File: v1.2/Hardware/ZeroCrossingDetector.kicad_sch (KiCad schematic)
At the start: 15 parts, among them Q17 MMBT3904, U12 OPA228

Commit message: Addition of firmware to v1.2(not tested)
+Addition of power tracking(with duty cycle control).
+Addition of resonance freq tracking(via proprietary algorithm relied on active and reactive power measurements)
+Quality factor monitoring
+Power boost when loaded(idle and loaded modes)
+Much better frequency resolution(less than 1Hz)
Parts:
- R49, R50: Link (none) -> https://ozdisan.com/passive-components/resistors/smt-smd-an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; Price 0.01964TL -> (none)

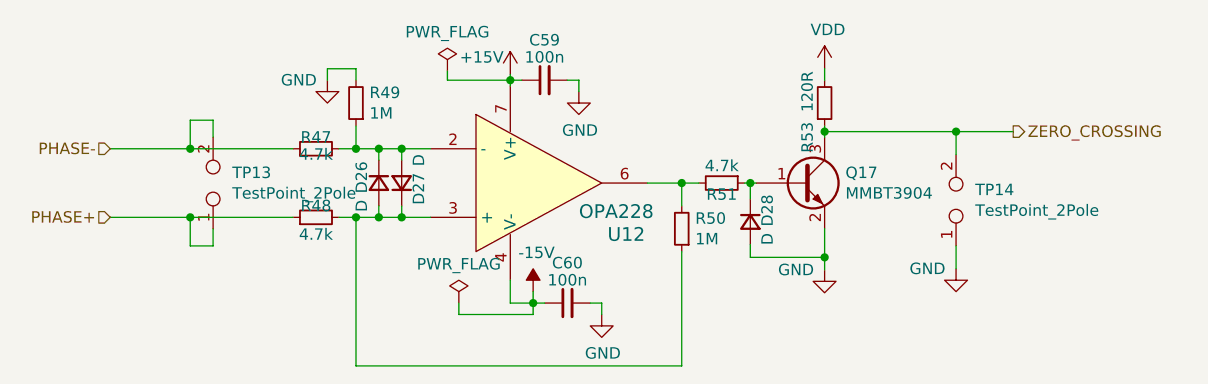
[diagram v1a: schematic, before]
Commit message: Start of rs485 communication interface development.
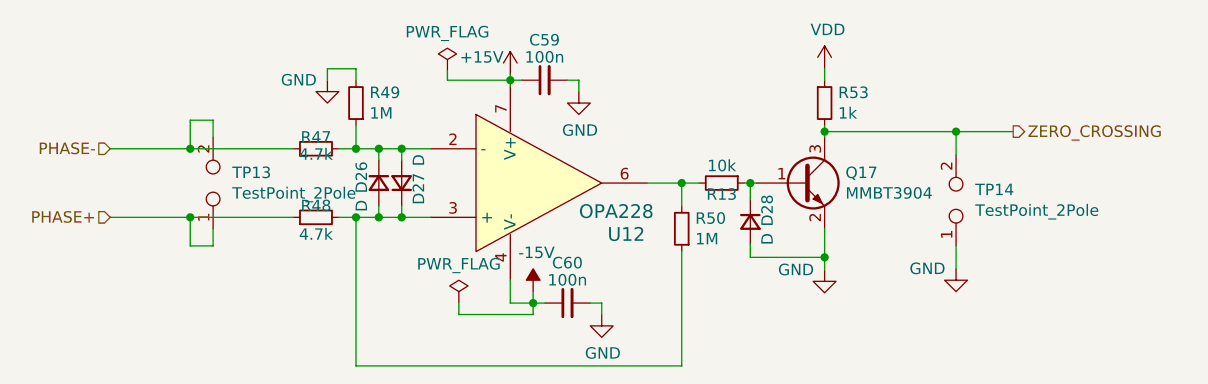
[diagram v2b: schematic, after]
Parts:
- removed R51: 4.7k, Resistor_SMD:R_0805_2012Metric, symbol Device:R_Small
- added R13: 10k, Resistor_SMD:R_0805_2012Metric, symbol Device:R_Small
- R53: value 120R -> 1k; footprint Resistor_SMD:R_0805_2012Metric -> Resistor_THT:R_Axial_DIN0204_L3.6mm_D1.6mm_P5.08mm_Horizontal; Link https://ozdisan.com/passive-components/resistors/smt-smd-an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 -> https://ozdisan.com/passive-components/resistors/tht-throug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; Price 0.01492TL -> 0.03898TL
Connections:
- net VDD: now also R53.1; no longer R53.2
- net ZERO_CROSSING: now also R53.2; no longer R53.1
- net at R50.2, U12.6: now also R13.2
- net at D28.1 (K), Q17.1 (B): now also R13.1
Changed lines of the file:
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@@
 (kicad_sch (version 20200618) (host eeschema "5.99.0-unknown-f3f1740~101~ubuntu18.04.1")
-  (page 1 8)
+  (page 8 8)
   (paper "A4")
   (junction (at 98.425 83.82) (diameter 0) (color 0 0 0 0))
@@
     (effects (font (size 1.27 1.27)) (justify left))
   )
-  (symbol (lib_id "power:PWR_FLAG") (at 127 75.184 0) (unit 1)
+  (symbol (lib_id "power:PWR_FLAG") (at 127 75.184 0)
     (in_bom yes) (on_board yes)
     (property "Reference" "#FLG0123" (id 0) (at 127 73.279 0)
@@
     )
   )
-  (symbol (lib_id "power:PWR_FLAG") (at 128.27 100.965 0) (unit 1)
+  (symbol (lib_id "power:PWR_FLAG") (at 128.27 100.965 0)
     (in_bom yes) (on_board yes)
     (property "Reference" "#FLG0122" (id 0) (at 128.27 99.06 0)
@@
     )
   )
-  (symbol (lib_id "power:+15V") (at 133.985 75.565 0) (unit 1)
+  (symbol (lib_id "power:+15V") (at 133.985 75.565 0)
     (in_bom yes) (on_board yes)
     (property "Reference" "#PWR059" (id 0) (at 133.985 79.375 0)
@@
     )
   )
-  (symbol (lib_id "power:-15V") (at 136.525 99.695 0) (unit 1)
+  (symbol (lib_id "power:-15V") (at 136.525 99.695 0)
     (in_bom yes) (on_board yes)
     (property "Reference" "#PWR060" (id 0) (at 136.525 97.155 0)
@@
     )
   )
-  (symbol (lib_id "power:VDD") (at 168.91 74.93 0) (unit 1)
+  (symbol (lib_id "power:VDD") (at 168.91 74.93 0)
     (in_bom yes) (on_board yes)
     (property "Reference" "#PWR075" (id 0) (at 168.91 78.74 0)
@@
     )
   )
-  (symbol (lib_id "power:GND") (at 113.665 76.2 0) (unit 1)
+  (symbol (lib_id "power:GND") (at 113.665 76.2 0)
     (in_bom yes) (on_board yes)
     (property "Reference" "#PWR058" (id 0) (at 113.665 82.55 0)
@@
     )
   )
-  (symbol (lib_id "power:GND") (at 141.605 77.47 0) (unit 1)
+  (symbol (lib_id "power:GND") (at 141.605 77.47 0)
     (in_bom yes) (on_board yes)
     (property "Reference" "#PWR061" (id 0) (at 141.605 83.82 0)
@@
     )
   )
-  (symbol (lib_id "power:GND") (at 144.145 102.235 0) (unit 1)
+  (symbol (lib_id "power:GND") (at 144.145 102.235 0)
     (in_bom yes) (on_board yes)
     (property "Reference" "#PWR062" (id 0) (at 144.145 108.585 0)
@@
     )
   )
-  (symbol (lib_id "power:GND") (at 168.91 97.282 0) (unit 1)
+  (symbol (lib_id "power:GND") (at 168.91 97.282 0)
     (in_bom yes) (on_board yes)
     (property "Reference" "#PWR065" (id 0) (at 168.91 103.632 0)
@@
     )
   )
-  (symbol (lib_id "power:GND") (at 183.515 97.155 0) (unit 1)
+  (symbol (lib_id "power:GND") (at 183.515 97.155 0)
     (in_bom yes) (on_board yes)
     (property "Reference" "#PWR0133" (id 0) (at 183.515 103.505 0)
@@
     )
   )
-  (symbol (lib_id "Device:R_Small") (at 112.395 83.82 90) (unit 1)
+  (symbol (lib_id "Device:R_Small") (at 112.395 83.82 90)
     (in_bom yes) (on_board yes)
     (property "Reference" "R47" (id 0) (at 112.395 82.55 90))
@@
     )
   )
-  (symbol (lib_id "Device:R_Small") (at 112.395 91.44 90) (unit 1)
+  (symbol (lib_id "Device:R_Small") (at 112.395 91.44 90)
     (in_bom yes) (on_board yes)
     (property "Reference" "R48" (id 0) (at 112.395 90.17 90))
@@
     )
   )
-  (symbol (lib_name "Device:R_Small_2") (lib_id "Device:R_Small") (at 116.84 78.74 180) (unit 1)
+  (symbol (lib_name "Device:R_Small_2") (lib_id "Device:R_Small") (at 116.84 78.74 180)
     (in_bom yes) (on_board yes)
     (property "Reference" "R49" (id 0) (at 118.3386 77.597 0)
@@
     )
   )
-  (symbol (lib_name "Device:R_Small_3") (lib_id "Device:R_Small") (at 153.035 92.71 180) (unit 1)
+  (symbol (lib_name "Device:R_Small_3") (lib_id "Device:R_Small") (at 153.035 92.71 180)
     (in_bom yes) (on_board yes)
     (property "Reference" "R50" (id 0) (at 154.5336 91.567 0)
@@
     )
   )
-  (symbol (lib_id "Device:R_Small") (at 157.48 87.63 270) (unit 1)
-    (in_bom yes) (on_board yes)
-    (property "Reference" "R51" (id 0) (at 157.48 88.9 90))
-    (property "Value" "4.7k" (id 1) (at 157.48 85.725 90))
+  (symbol (lib_name "Device:R_Small_7") (lib_id "Device:R_Small") (at 157.48 87.63 270)
+    (in_bom yes) (on_board yes)
+    (property "Reference" "R13" (id 0) (at 157.48 88.9 90))
+    (property "Value" "10k" (id 1) (at 157.48 85.725 90))
     (property "Footprint" "Resistor_SMD:R_0805_2012Metric" (id 2) (at 157.48 87.63 0)
       (effects (font (size 1.27 1.27)) hide)
@@
       (effects (font (size 1.27 1.27)) hide)
     )
-    (property "Link" "https://ozdisan.com/passive-components/resistors/smt-smd-and-chip-resistors/0805S8F4701T5E" (id 4) (at 157.48 87.63 90)
-      (effects (font (size 1.27 1.27)) hide)
-    )
-    (property "Price" "0.01955TL" (id 5) (at 157.48 87.63 90)
-      (effects (font (size 1.27 1.27)) hide)
-    )
-  )
-  (symbol (lib_name "Device:R_Small_1") (lib_id "Device:R_Small") (at 168.91 78.74 0) (mirror x) (unit 1)
-    (in_bom yes) (on_board yes)
-    (property "Reference" "R53" (id 0) (at 167.005 82.55 90))
-    (property "Value" "120R" (id 1) (at 167.005 77.47 90))
-    (property "Footprint" "Resistor_SMD:R_0805_2012Metric" (id 2) (at 168.91 78.74 0)
+    (property "Link" "https://ozdisan.com/passive-components/resistors/smt-smd-and-chip-resistors/0805S8J0103T5E" (id 4) (at 157.48 87.63 90)
+      (effects (font (size 1.27 1.27)) hide)
+    )
+    (property "Price" "0.01518TL" (id 5) (at 157.48 87.63 90)
+      (effects (font (size 1.27 1.27)) hide)
+    )
+  )
+  (symbol (lib_name "Device:R_Small_4") (lib_id "Device:R_Small") (at 168.91 78.74 0) (unit 1)
+    (in_bom yes) (on_board yes)
+    (property "Reference" "R53" (id 0) (at 170.4086 77.597 0)
+      (effects (font (size 1.27 1.27)) (justify left))
+    )
+    (property "Value" "1k" (id 1) (at 170.4086 79.883 0)
+      (effects (font (size 1.27 1.27)) (justify left))
+    )
+    (property "Footprint" "Resistor_THT:R_Axial_DIN0204_L3.6mm_D1.6mm_P5.08mm_Horizontal" (id 2) (at 168.91 78.74 0)
       (effects (font (size 1.27 1.27)) hide)
     )
@@
       (effects (font (size 1.27 1.27)) hide)
     )
-    (property "Link" "https://ozdisan.com/passive-components/resistors/smt-smd-and-chip-resistors/0805S8J0121T5E" (id 4) (at 168.91 78.74 90)
-      (effects (font (size 1.27 1.27)) hide)
-    )
-    (property "Price" "0.01492TL" (id 5) (at 168.91 78.74 90)
-      (effects (font (size 1.27 1.27)) hide)
-    )
-  )
-  (symbol (lib_id "Device:D_Small") (at 119.38 87.63 90) (mirror x) (unit 1)
+    (property "Link" "https://ozdisan.com/passive-components/resistors/tht-through-hole-resistors/CFR0W8J0102A50" (id 4) (at 168.91 78.74 0)
+      (effects (font (size 1.27 1.27)) hide)
+    )
+    (property "Price" "0.03898TL" (id 5) (at 168.91 78.74 0)
+      (effects (font (size 1.27 1.27)) hide)
+    )
+  )
+  (symbol (lib_id "Device:D_Small") (at 119.38 87.63 90) (mirror x)
     (in_bom yes) (on_board yes)
     (property "Reference" "D26" (id 0) (at 117.475 86.995 0))
@@
     )
   )
-  (symbol (lib_name "Device:D_Small_3") (lib_id "Device:D_Small") (at 121.92 87.63 270) (mirror x) (unit 1)
+  (symbol (lib_name "Device:D_Small_3") (lib_id "Device:D_Small") (at 121.92 87.63 270) (mirror x)
     (in_bom yes) (on_board yes)
     (property "Reference" "D27" (id 0) (at 123.825 88.265 0))
@@
     )
   )
-  (symbol (lib_name "Device:D_Small_1") (lib_id "Device:D_Small") (at 160.655 91.948 90) (mirror x) (unit 1)
+  (symbol (lib_name "Device:D_Small_1") (lib_id "Device:D_Small") (at 160.655 91.948 90) (mirror x)
     (in_bom yes) (on_board yes)
     (property "Reference" "D28" (id 0) (at 162.56 90.678 0))
@@
     )
   )
-  (symbol (lib_id "Device:C_Small") (at 137.795 76.2 90) (unit 1)
+  (symbol (lib_id "Device:C_Small") (at 137.795 76.2 90)
     (in_bom yes) (on_board yes)
     (property "Reference" "C59" (id 0) (at 137.795 71.755 90))
@@
     )
   )
-  (symbol (lib_id "Device:C_Small") (at 140.335 100.965 90) (unit 1)
+  (symbol (lib_id "Device:C_Small") (at 140.335 100.965 90)
     (in_bom yes) (on_board yes)
     (property "Reference" "C60" (id 0) (at 140.335 96.52 90))
@@
     )
   )
-  (symbol (lib_id "Connector:TestPoint_2Pole") (at 100.965 87.63 90) (unit 1)
+  (symbol (lib_id "Connector:TestPoint_2Pole") (at 100.965 87.63 90)
     (in_bom yes) (on_board yes)
     (property "Reference" "TP13" (id 0) (at 103.0986 86.487 90)
@@
     )
   )
-  (symbol (lib_name "Connector:TestPoint_2Pole_1") (lib_id "Connector:TestPoint_2Pole") (at 183.515 89.535 90) (unit 1)
+  (symbol (lib_name "Connector:TestPoint_2Pole_1") (lib_id "Connector:TestPoint_2Pole") (at 183.515 89.535 90)
     (in_bom yes) (on_board yes)
     (property "Reference" "TP14" (id 0) (at 185.6487 88.3856 90)
@@
     )
   )
-  (symbol (lib_id "Transistor_BJT:MMBT3904") (at 166.37 87.63 0) (unit 1)
+  (symbol (lib_id "Transistor_BJT:MMBT3904") (at 166.37 87.63 0)
     (in_bom yes) (on_board yes)
     (property "Reference" "Q17" (id 0) (at 171.2214 86.487 0)
@@
     )
   )
-  (symbol (lib_id "oe_opamp:OPA228") (at 135.89 87.63 0) (unit 1)
+  (symbol (lib_id "oe_opamp:OPA228") (at 135.89 87.63 0)
     (in_bom yes) (on_board yes)
     (property "Reference" "U12" (id 0) (at 144.78 93.345 0)

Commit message: Redesign.
+Cli interface.
+Modularity improvement(complex number and pid modules created)
+Range change.
+Core-Lattice seperated. 
+Improvement of the control function
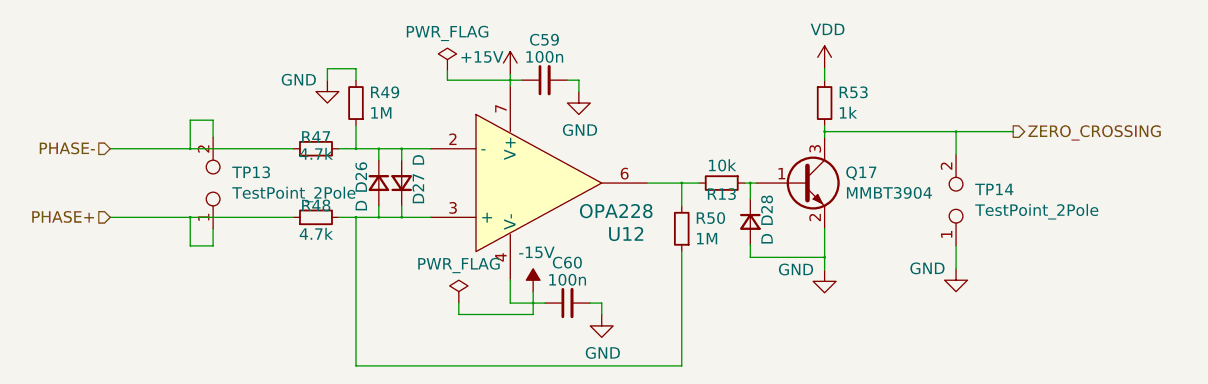
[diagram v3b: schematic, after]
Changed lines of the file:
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@@
-(kicad_sch (version 20200618) (host eeschema "5.99.0-unknown-f3f1740~101~ubuntu18.04.1")
+(kicad_sch (version 20200828) (generator eeschema)
   (page 8 8)
   (paper "A4")
-  (junction (at 98.425 83.82) (diameter 0) (color 0 0 0 0))
-  (junction (at 98.425 91.44) (diameter 0) (color 0 0 0 0))
-  (junction (at 116.84 83.82) (diameter 0) (color 0 0 0 0))
-  (junction (at 116.84 91.44) (diameter 0) (color 0 0 0 0))
-  (junction (at 119.38 83.82) (diameter 0) (color 0 0 0 0))
-  (junction (at 119.38 91.44) (diameter 0) (color 0 0 0 0))
-  (junction (at 121.92 83.82) (diameter 0) (color 0 0 0 0))
-  (junction (at 121.92 91.44) (diameter 0) (color 0 0 0 0))
-  (junction (at 133.985 76.2) (diameter 0) (color 0 0 0 0))
-  (junction (at 136.525 100.965) (diameter 0) (color 0 0 0 0))
-  (junction (at 153.035 87.63) (diameter 0) (color 0 0 0 0))
-  (junction (at 160.655 87.63) (diameter 0) (color 0 0 0 0))
-  (junction (at 168.91 81.915) (diameter 0) (color 0 0 0 0))
-  (junction (at 168.91 95.885) (diameter 0) (color 0 0 0 0))
-  (junction (at 183.515 81.915) (diameter 0) (color 0 0 0 0))
+  (junction (at 98.425 83.82) (diameter 0.3048) (color 0 0 0 0))
+  (junction (at 98.425 91.44) (diameter 0.3048) (color 0 0 0 0))
+  (junction (at 116.84 83.82) (diameter 0.3048) (color 0 0 0 0))
+  (junction (at 116.84 91.44) (diameter 0.3048) (color 0 0 0 0))
+  (junction (at 119.38 83.82) (diameter 0.3048) (color 0 0 0 0))
+  (junction (at 119.38 91.44) (diameter 0.3048) (color 0 0 0 0))
+  (junction (at 121.92 83.82) (diameter 0.3048) (color 0 0 0 0))
+  (junction (at 121.92 91.44) (diameter 0.3048) (color 0 0 0 0))
+  (junction (at 133.985 76.2) (diameter 0.3048) (color 0 0 0 0))
+  (junction (at 136.525 100.965) (diameter 0.3048) (color 0 0 0 0))
+  (junction (at 153.035 87.63) (diameter 0.3048) (color 0 0 0 0))
+  (junction (at 160.655 87.63) (diameter 0.3048) (color 0 0 0 0))
+  (junction (at 168.91 81.915) (diameter 0.3048) (color 0 0 0 0))
+  (junction (at 168.91 95.885) (diameter 0.3048) (color 0 0 0 0))
+  (junction (at 183.515 81.915) (diameter 0.3048) (color 0 0 0 0))
   (wire (pts (xy 89.535 83.82) (xy 98.425 83.82))
     (stroke (width 0) (type solid) (color 0 0 0 0))
@@
     (effects (font (size 1.27 1.27)) (justify left))
   )
-  (symbol (lib_id "power:PWR_FLAG") (at 127 75.184 0)
+  (symbol (lib_id "power:PWR_FLAG") (at 127 75.184 0) (unit 1)
     (in_bom yes) (on_board yes)
     (property "Reference" "#FLG0123" (id 0) (at 127 73.279 0)
@@
     )
   )
-  (symbol (lib_id "power:PWR_FLAG") (at 128.27 100.965 0)
+  (symbol (lib_id "power:PWR_FLAG") (at 128.27 100.965 0) (unit 1)
     (in_bom yes) (on_board yes)
     (property "Reference" "#FLG0122" (id 0) (at 128.27 99.06 0)
@@
     )
   )
-  (symbol (lib_id "power:+15V") (at 133.985 75.565 0)
+  (symbol (lib_id "power:+15V") (at 133.985 75.565 0) (unit 1)
     (in_bom yes) (on_board yes)
     (property "Reference" "#PWR059" (id 0) (at 133.985 79.375 0)
@@
     )
   )
-  (symbol (lib_id "power:-15V") (at 136.525 99.695 0)
+  (symbol (lib_id "power:-15V") (at 136.525 99.695 0) (unit 1)
     (in_bom yes) (on_board yes)
     (property "Reference" "#PWR060" (id 0) (at 136.525 97.155 0)
@@
     )
   )
-  (symbol (lib_id "power:VDD") (at 168.91 74.93 0)
+  (symbol (lib_id "power:VDD") (at 168.91 74.93 0) (unit 1)
     (in_bom yes) (on_board yes)
     (property "Reference" "#PWR075" (id 0) (at 168.91 78.74 0)
@@
     )
   )
-  (symbol (lib_id "power:GND") (at 113.665 76.2 0)
+  (symbol (lib_id "power:GND") (at 113.665 76.2 0) (unit 1)
     (in_bom yes) (on_board yes)
     (property "Reference" "#PWR058" (id 0) (at 113.665 82.55 0)
@@
     )
   )
-  (symbol (lib_id "power:GND") (at 141.605 77.47 0)
+  (symbol (lib_id "power:GND") (at 141.605 77.47 0) (unit 1)
     (in_bom yes) (on_board yes)
     (property "Reference" "#PWR061" (id 0) (at 141.605 83.82 0)
@@
     )
   )
-  (symbol (lib_id "power:GND") (at 144.145 102.235 0)
+  (symbol (lib_id "power:GND") (at 144.145 102.235 0) (unit 1)
     (in_bom yes) (on_board yes)
     (property "Reference" "#PWR062" (id 0) (at 144.145 108.585 0)
@@
     )
   )
-  (symbol (lib_id "power:GND") (at 168.91 97.282 0)
+  (symbol (lib_id "power:GND") (at 168.91 97.282 0) (unit 1)
     (in_bom yes) (on_board yes)
     (property "Reference" "#PWR065" (id 0) (at 168.91 103.632 0)
@@
     )
   )
-  (symbol (lib_id "power:GND") (at 183.515 97.155 0)
+  (symbol (lib_id "power:GND") (at 183.515 97.155 0) (unit 1)
     (in_bom yes) (on_board yes)
     (property "Reference" "#PWR0133" (id 0) (at 183.515 103.505 0)
@@
     )
   )
-  (symbol (lib_id "Device:R_Small") (at 112.395 83.82 90)
+  (symbol (lib_id "Device:R_Small") (at 112.395 83.82 90) (unit 1)
     (in_bom yes) (on_board yes)
     (property "Reference" "R47" (id 0) (at 112.395 82.55 90))
@@
     )
   )
-  (symbol (lib_id "Device:R_Small") (at 112.395 91.44 90)
+  (symbol (lib_id "Device:R_Small") (at 112.395 91.44 90) (unit 1)
     (in_bom yes) (on_board yes)
     (property "Reference" "R48" (id 0) (at 112.395 90.17 90))
@@
     )
   )
-  (symbol (lib_name "Device:R_Small_2") (lib_id "Device:R_Small") (at 116.84 78.74 180)
+  (symbol (lib_name "Device:R_Small_2") (lib_id "Device:R_Small") (at 116.84 78.74 180) (unit 1)
     (in_bom yes) (on_board yes)
     (property "Reference" "R49" (id 0) (at 118.3386 77.597 0)
@@
     )
   )
-  (symbol (lib_name "Device:R_Small_3") (lib_id "Device:R_Small") (at 153.035 92.71 180)
+  (symbol (lib_name "Device:R_Small_3") (lib_id "Device:R_Small") (at 153.035 92.71 180) (unit 1)
     (in_bom yes) (on_board yes)
     (property "Reference" "R50" (id 0) (at 154.5336 91.567 0)
@@
     )
   )
-  (symbol (lib_name "Device:R_Small_7") (lib_id "Device:R_Small") (at 157.48 87.63 270)
+  (symbol (lib_name "Device:R_Small_7") (lib_id "Device:R_Small") (at 157.48 87.63 270) (unit 1)
     (in_bom yes) (on_board yes)
     (property "Reference" "R13" (id 0) (at 157.48 88.9 90))
@@
     )
   )
-  (symbol (lib_id "Device:D_Small") (at 119.38 87.63 90) (mirror x)
+  (symbol (lib_id "Device:D_Small") (at 119.38 87.63 90) (mirror x) (unit 1)
     (in_bom yes) (on_board yes)
     (property "Reference" "D26" (id 0) (at 117.475 86.995 0))
@@
     )
   )
-  (symbol (lib_name "Device:D_Small_3") (lib_id "Device:D_Small") (at 121.92 87.63 270) (mirror x)
+  (symbol (lib_name "Device:D_Small_3") (lib_id "Device:D_Small") (at 121.92 87.63 270) (mirror x) (unit 1)
     (in_bom yes) (on_board yes)
     (property "Reference" "D27" (id 0) (at 123.825 88.265 0))
@@
     )
   )
-  (symbol (lib_name "Device:D_Small_1") (lib_id "Device:D_Small") (at 160.655 91.948 90) (mirror x)
+  (symbol (lib_name "Device:D_Small_1") (lib_id "Device:D_Small") (at 160.655 91.948 90) (mirror x) (unit 1)
     (in_bom yes) (on_board yes)
     (property "Reference" "D28" (id 0) (at 162.56 90.678 0))
@@
     )
   )
-  (symbol (lib_id "Device:C_Small") (at 137.795 76.2 90)
+  (symbol (lib_id "Device:C_Small") (at 137.795 76.2 90) (unit 1)
     (in_bom yes) (on_board yes)
     (property "Reference" "C59" (id 0) (at 137.795 71.755 90))
@@
     )
   )
-  (symbol (lib_id "Device:C_Small") (at 140.335 100.965 90)
+  (symbol (lib_id "Device:C_Small") (at 140.335 100.965 90) (unit 1)
     (in_bom yes) (on_board yes)
     (property "Reference" "C60" (id 0) (at 140.335 96.52 90))
@@
     )
   )
-  (symbol (lib_id "Connector:TestPoint_2Pole") (at 100.965 87.63 90)
+  (symbol (lib_id "Connector:TestPoint_2Pole") (at 100.965 87.63 90) (unit 1)
     (in_bom yes) (on_board yes)
     (property "Reference" "TP13" (id 0) (at 103.0986 86.487 90)
@@
     )
   )
-  (symbol (lib_name "Connector:TestPoint_2Pole_1") (lib_id "Connector:TestPoint_2Pole") (at 183.515 89.535 90)
+  (symbol (lib_name "Connector:TestPoint_2Pole_1") (lib_id "Connector:TestPoint_2Pole") (at 183.515 89.535 90) (unit 1)
     (in_bom yes) (on_board yes)
     (property "Reference" "TP14" (id 0) (at 185.6487 88.3856 90)
@@
     )
   )
-  (symbol (lib_id "Transistor_BJT:MMBT3904") (at 166.37 87.63 0)
+  (symbol (lib_id "Transistor_BJT:MMBT3904") (at 166.37 87.63 0) (unit 1)
     (in_bom yes) (on_board yes)
     (property "Reference" "Q17" (id 0) (at 171.2214 86.487 0)
@@
     )
   )
-  (symbol (lib_id "oe_opamp:OPA228") (at 135.89 87.63 0)
+  (symbol (lib_id "oe_opamp:OPA228") (at 135.89 87.63 0) (unit 1)
     (in_bom yes) (on_board yes)
     (property "Reference" "U12" (id 0) (at 144.78 93.345 0)
